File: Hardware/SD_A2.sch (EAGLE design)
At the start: 24 parts, among them IC1 74LS245N, IC2 LM1117DTX-3.3, IC3 28C64ASO, IC4 XC9572XL

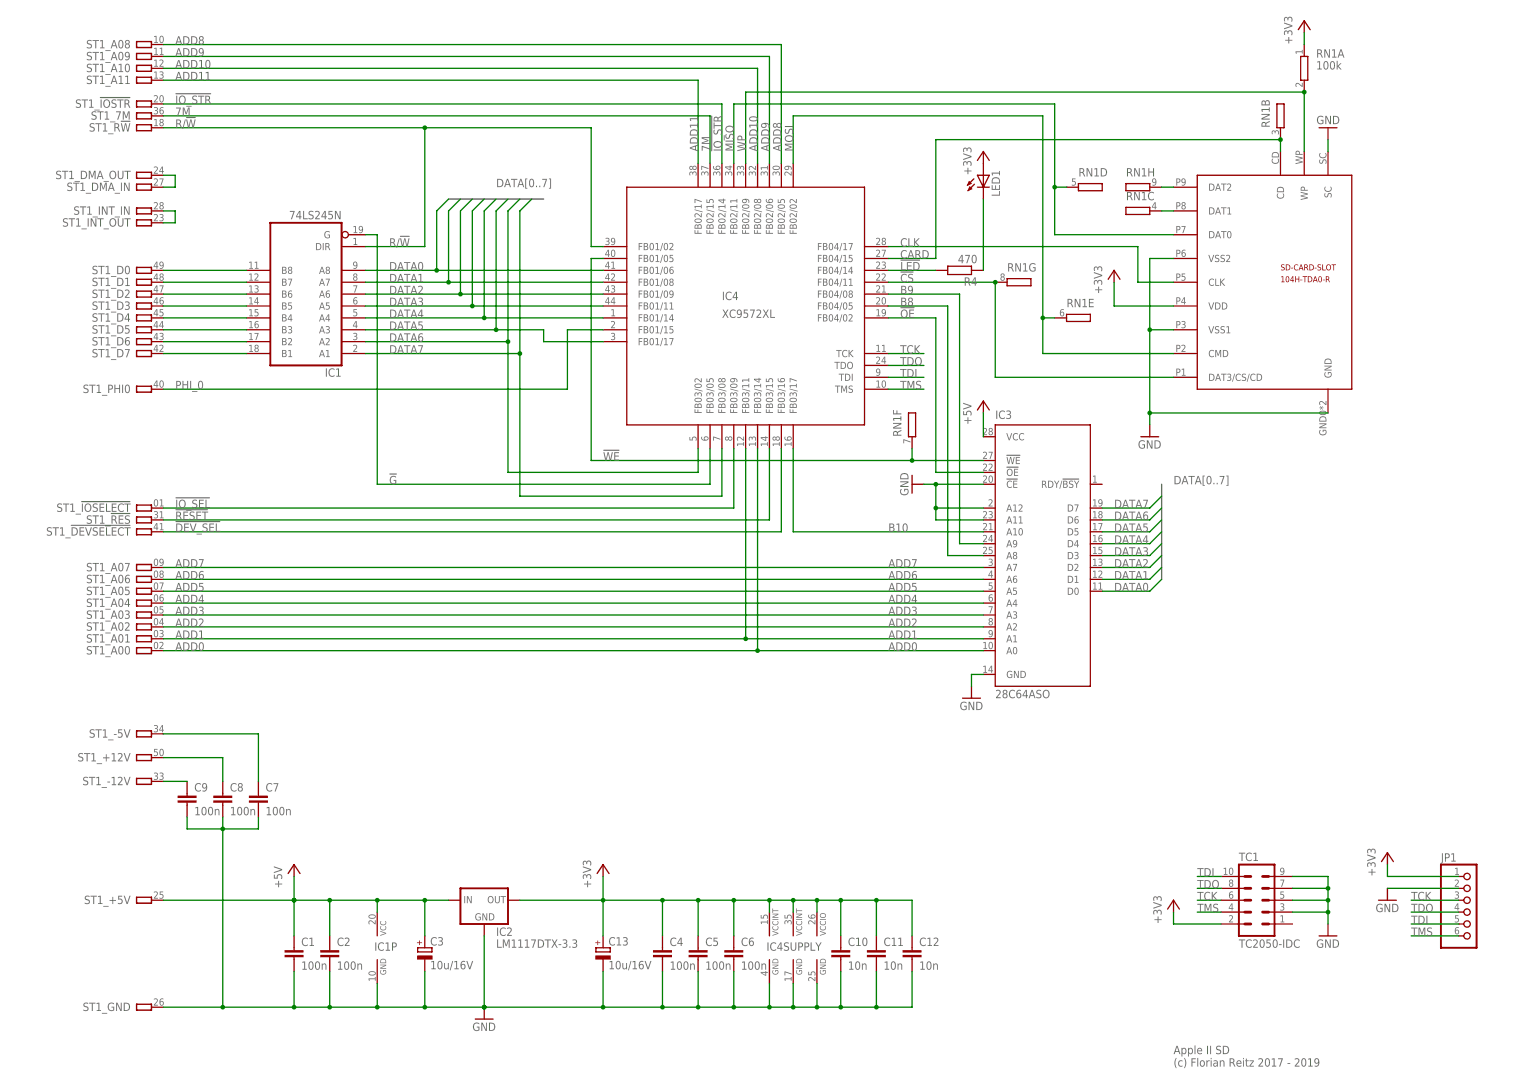
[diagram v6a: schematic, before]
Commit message: R/W jumper re-added
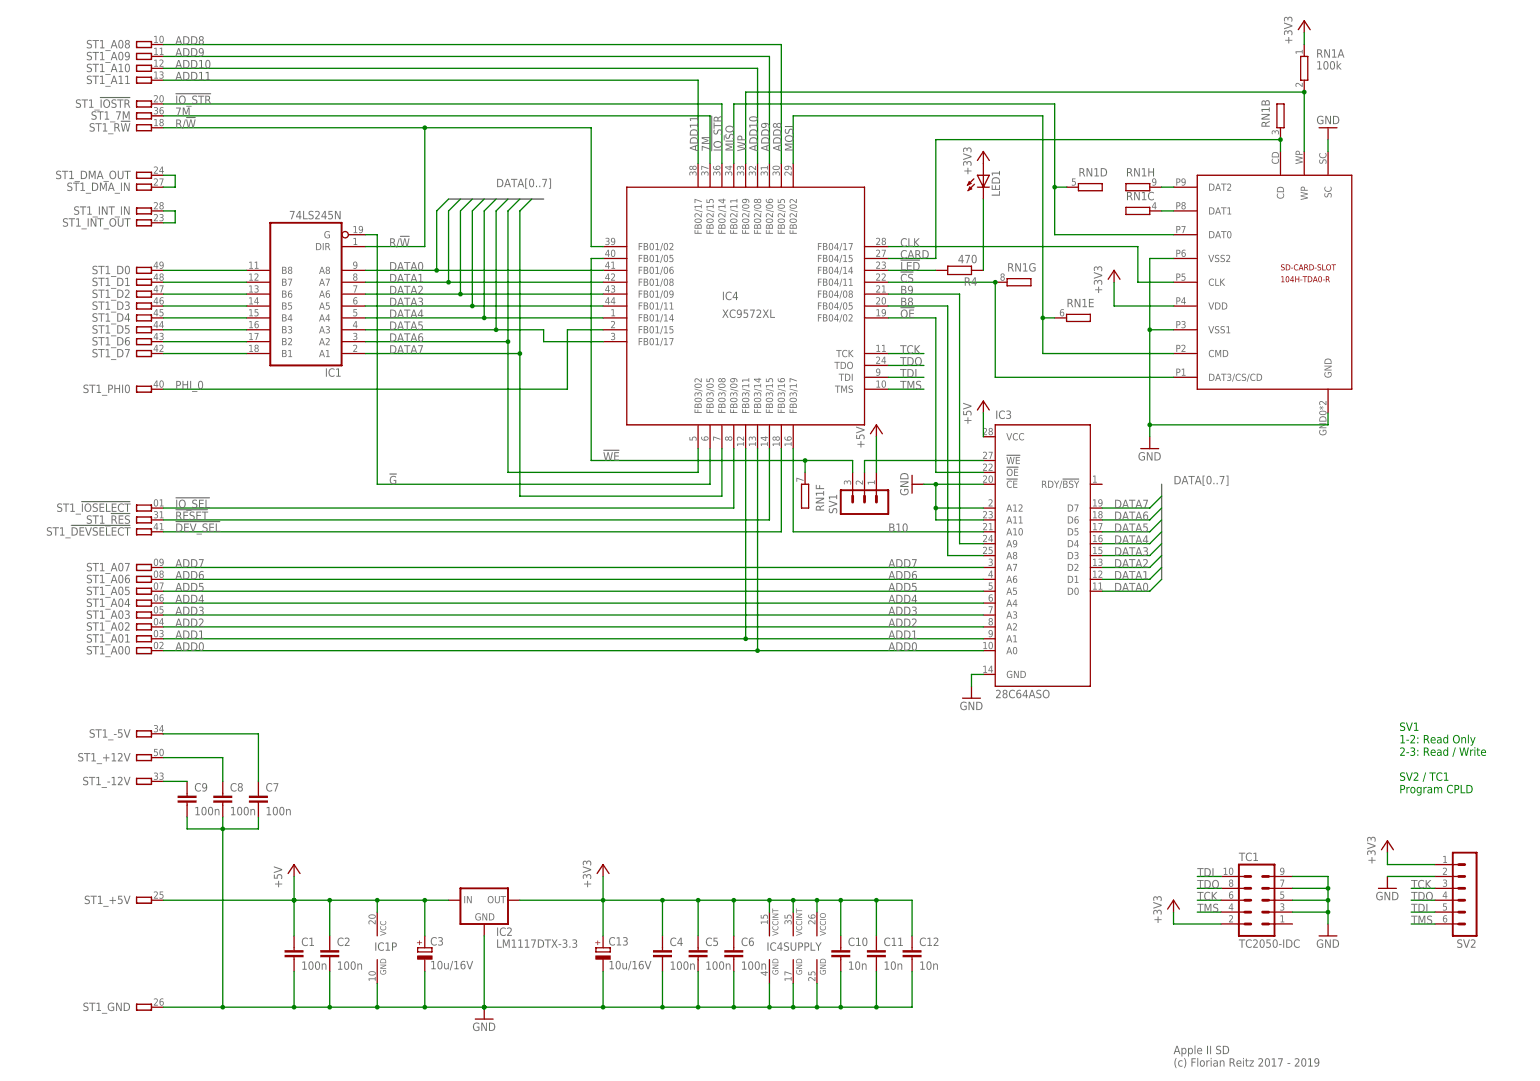
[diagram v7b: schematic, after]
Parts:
- removed JP1: (no value), pinhead:PINHD-1X6
- added SV1: (no value), con-lstb:MA03-1
- added SV2: (no value), con-lstb:MA06-1
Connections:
- new net N$1: IC3.!WE, SV1.2
- net !WE: now also SV1.3; no longer IC3.!WE
- net +3V3: now also SV2.1; no longer JP1.1
- net +5V: now also SV1.1
- net GND: now also SV2.2; no longer JP1.2
- net TCK: now also SV2.3; no longer JP1.3
- net TDI: now also SV2.5; no longer JP1.5
- net TDO: now also SV2.4; no longer JP1.4
- net TMS: now also SV2.6; no longer JP1.6
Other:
- note added: "SV1 1-2: Read Only 2-3: Read / Write SV2 / TC1 Program CPLD"
- moved on the sheet: RN1F
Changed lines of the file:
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@@
 <part name="C3" library="rcl@1" deviceset="CPOL-EU" device="A/3216-18R" value="10u/16V"/>
 <part name="C13" library="rcl@1" deviceset="CPOL-EU" device="A/3216-18R" value="10u/16V"/>
-<part name="JP1" library="pinhead" deviceset="PINHD-1X6" device=""/>
-<part name="+3V2" library="supply1" deviceset="+3V3" device=""/>
-<part name="GND2" library="supply1" deviceset="GND" device=""/>
 <part name="TC1" library="TagConnect" deviceset="TC2050-IDC" device=""/>
+<part name="SV1" library="con-lstb" deviceset="MA03-1" device=""/>
+<part name="SV2" library="con-lstb" deviceset="MA06-1" device=""/>
+<part name="P+2" library="supply1" deviceset="+5V" device=""/>
+<part name="+3V7" library="supply1" deviceset="+3V3" device=""/>
+<part name="GND3" library="supply1" deviceset="GND" device=""/>
 </parts>
 <sheets>
@@
 <text x="261.62" y="-27.94" size="1.778" layer="95" font="vector">Apple II SD
 (c) Florian Reitz 2017 - 2019</text>
+<text x="309.88" y="30.48" size="1.778" layer="91">SV1
+1-2: Read Only
+2-3: Read / Write
+SV2 / TC1
+Program CPLD</text>
 </plain>
 <instances>
@@
 <attribute name="NAME" x="174.625" y="-3.175" size="1.778" layer="95"/>
 </instance>
-<instance part="GND6" gate="1" x="256.54" y="106.68"/>
+<instance part="GND6" gate="1" x="256.54" y="104.14"/>
 <instance part="R4" gate="G$1" x="215.9" y="142.24" rot="R180"/>
 <instance part="+3V4" gate="G$1" x="220.98" y="167.64"/>
@@
 <instance part="C3" gate="G$1" x="101.6" y="-2.54"/>
 <instance part="C13" gate="G$1" x="139.7" y="-2.54"/>
-<instance part="RN1" gate="F" x="205.74" y="109.22" smashed="yes">
-<attribute name="NAME" x="203.454" y="106.68" size="1.778" layer="95" rot="R90"/>
+<instance part="RN1" gate="F" x="182.88" y="93.98" smashed="yes" rot="R180">
+<attribute name="NAME" x="185.166" y="96.52" size="1.778" layer="95" rot="R270"/>
 </instance>
-<instance part="JP1" gate="A" x="325.12" y="5.08"/>
-<instance part="+3V2" gate="G$1" x="307.34" y="17.78"/>
-<instance part="GND2" gate="1" x="307.34" y="7.62"/>
 <instance part="TC1" gate="A" x="279.4" y="7.62"/>
+<instance part="SV1" gate="G$1" x="195.58" y="91.44" rot="R90"/>
+<instance part="SV2" gate="1" x="325.12" y="7.62" rot="R180"/>
+<instance part="P+2" gate="1" x="198.12" y="109.22"/>
+<instance part="+3V7" gate="G$1" x="307.34" y="20.32"/>
+<instance part="GND3" gate="1" x="307.34" y="10.16"/>
 </instances>
 <busses>
@@
 <wire x1="256.54" y1="144.78" x2="256.54" y2="129.54" width="0.1524" layer="91"/>
 <pinref part="U$2" gate="G$1" pin="VSS1"/>
-<wire x1="256.54" y1="129.54" x2="256.54" y2="111.76" width="0.1524" layer="91"/>
-<wire x1="256.54" y1="111.76" x2="256.54" y2="109.22" width="0.1524" layer="91"/>
+<wire x1="256.54" y1="129.54" x2="256.54" y2="109.22" width="0.1524" layer="91"/>
+<wire x1="256.54" y1="109.22" x2="256.54" y2="106.68" width="0.1524" layer="91"/>
 <wire x1="261.62" y1="129.54" x2="256.54" y2="129.54" width="0.1524" layer="91"/>
 <junction x="256.54" y="129.54"/>
 <pinref part="U$2" gate="G$1" pin="GND"/>
-<wire x1="294.64" y1="111.76" x2="256.54" y2="111.76" width="0.1524" layer="91"/>
-<junction x="256.54" y="111.76"/>
+<wire x1="294.64" y1="111.76" x2="294.64" y2="109.22" width="0.1524" layer="91"/>
+<wire x1="294.64" y1="109.22" x2="256.54" y2="109.22" width="0.1524" layer="91"/>
+<junction x="256.54" y="109.22"/>
 </segment>
 <segment>
@@
 <wire x1="220.98" y1="55.88" x2="218.44" y2="55.88" width="0.1524" layer="91"/>
 <wire x1="218.44" y1="55.88" x2="218.44" y2="53.34" width="0.1524" layer="91"/>
-</segment>
-<segment>
-<pinref part="JP1" gate="A" pin="2"/>
-<pinref part="GND2" gate="1" pin="GND"/>
-<wire x1="322.58" y1="10.16" x2="307.34" y2="10.16" width="0.1524" layer="91"/>
 </segment>
 <segment>
@@
 <junction x="294.64" y="7.62"/>
 <junction x="294.64" y="5.08"/>
+</segment>
+<segment>
+<pinref part="GND3" gate="1" pin="GND"/>
+<pinref part="SV2" gate="1" pin="2"/>
+<wire x1="307.34" y1="12.7" x2="317.5" y2="12.7" width="0.1524" layer="91"/>
 </segment>
 </net>
@@
 <pinref part="IC3" gate="G$1" pin="VCC"/>
 <wire x1="220.98" y1="111.76" x2="220.98" y2="106.68" width="0.1524" layer="91"/>
+</segment>
+<segment>
+<pinref part="SV1" gate="G$1" pin="1"/>
+<wire x1="198.12" y1="99.06" x2="198.12" y2="106.68" width="0.1524" layer="91"/>
+<pinref part="P+2" gate="1" pin="+5V"/>
 </segment>
 </net>
@@
 </segment>
 <segment>
-<pinref part="+3V2" gate="G$1" pin="+3V3"/>
-<wire x1="307.34" y1="15.24" x2="307.34" y2="12.7" width="0.1524" layer="91"/>
-<pinref part="JP1" gate="A" pin="1"/>
-<wire x1="307.34" y1="12.7" x2="322.58" y2="12.7" width="0.1524" layer="91"/>
-</segment>
-<segment>
 <pinref part="TC1" gate="A" pin="2"/>
 <pinref part="+3V6" gate="G$1" pin="+3V3"/>
 <wire x1="271.78" y1="2.54" x2="261.62" y2="2.54" width="0.1524" layer="91"/>
 <wire x1="261.62" y1="2.54" x2="261.62" y2="5.08" width="0.1524" layer="91"/>
+</segment>
+<segment>
+<pinref part="+3V7" gate="G$1" pin="+3V3"/>
+<wire x1="307.34" y1="17.78" x2="307.34" y2="15.24" width="0.1524" layer="91"/>
+<pinref part="SV2" gate="1" pin="1"/>
+<wire x1="307.34" y1="15.24" x2="317.5" y2="15.24" width="0.1524" layer="91"/>
 </segment>
 </net>
@@
 </segment>
 <segment>
-<pinref part="JP1" gate="A" pin="3"/>
-<wire x1="322.58" y1="7.62" x2="312.42" y2="7.62" width="0.1524" layer="91"/>
-<label x="312.42" y="7.62" size="1.778" layer="95"/>
-</segment>
-<segment>
 <pinref part="TC1" gate="A" pin="6"/>
 <wire x1="271.78" y1="7.62" x2="266.7" y2="7.62" width="0.1524" layer="91"/>
 <label x="266.7" y="7.62" size="1.778" layer="95"/>
 </segment>
+<segment>
+<pinref part="SV2" gate="1" pin="3"/>
+<wire x1="317.5" y1="10.16" x2="312.42" y2="10.16" width="0.1524" layer="91"/>
+<label x="312.42" y="10.16" size="1.778" layer="95"/>
+</segment>
 </net>
 <net name="TDO" class="0">
@@
 </segment>
 <segment>
-<pinref part="JP1" gate="A" pin="4"/>
-<wire x1="322.58" y1="5.08" x2="312.42" y2="5.08" width="0.1524" layer="91"/>
-<label x="312.42" y="5.08" size="1.778" layer="95"/>
-</segment>
-<segment>
 <pinref part="TC1" gate="A" pin="8"/>
 <wire x1="271.78" y1="10.16" x2="266.7" y2="10.16" width="0.1524" layer="91"/>
 <label x="266.7" y="10.16" size="1.778" layer="95"/>
 </segment>
+<segment>
+<pinref part="SV2" gate="1" pin="4"/>
+<wire x1="317.5" y1="7.62" x2="312.42" y2="7.62" width="0.1524" layer="91"/>
+<label x="312.42" y="7.62" size="1.778" layer="95"/>
+</segment>
 </net>
 <net name="TDI" class="0">
@@
 </segment>
 <segment>
-<pinref part="JP1" gate="A" pin="5"/>
-<wire x1="322.58" y1="2.54" x2="312.42" y2="2.54" width="0.1524" layer="91"/>
-<label x="312.42" y="2.54" size="1.778" layer="95"/>
-</segment>
-<segment>
 <pinref part="TC1" gate="A" pin="10"/>
 <wire x1="271.78" y1="12.7" x2="266.7" y2="12.7" width="0.1524" layer="91"/>
 <label x="266.7" y="12.7" size="1.778" layer="95"/>
 </segment>
+<segment>
+<pinref part="SV2" gate="1" pin="5"/>
+<wire x1="317.5" y1="5.08" x2="312.42" y2="5.08" width="0.1524" layer="91"/>
+<label x="312.42" y="5.08" size="1.778" layer="95"/>
+</segment>
 </net>
 <net name="TMS" class="0">
@@
 </segment>
 <segment>
-<pinref part="JP1" gate="A" pin="6"/>
-<wire x1="322.58" y1="0" x2="312.42" y2="0" width="0.1524" layer="91"/>
-<label x="312.42" y="0" size="1.778" layer="95"/>
-</segment>
-<segment>
 <pinref part="TC1" gate="A" pin="4"/>
 <wire x1="271.78" y1="5.08" x2="266.7" y2="5.08" width="0.1524" layer="91"/>
 <label x="266.7" y="5.08" size="1.778" layer="95"/>
+</segment>
+<segment>
+<pinref part="SV2" gate="1" pin="6"/>
+<wire x1="317.5" y1="2.54" x2="312.42" y2="2.54" width="0.1524" layer="91"/>
+<label x="312.42" y="2.54" size="1.778" layer="95"/>
 </segment>
 </net>
@@
 <wire x1="139.7" y1="144.78" x2="137.16" y2="144.78" width="0.1524" layer="91"/>
 <wire x1="137.16" y1="144.78" x2="137.16" y2="101.6" width="0.1524" layer="91"/>
-<wire x1="137.16" y1="101.6" x2="205.74" y2="101.6" width="0.1524" layer="91"/>
+<wire x1="137.16" y1="101.6" x2="182.88" y2="101.6" width="0.1524" layer="91"/>
 <label x="139.7" y="101.6" size="1.778" layer="95"/>
-<pinref part="IC3" gate="G$1" pin="!WE"/>
 <pinref part="RN1" gate="F" pin="2"/>
-<wire x1="205.74" y1="101.6" x2="220.98" y2="101.6" width="0.1524" layer="91"/>
-<wire x1="205.74" y1="104.14" x2="205.74" y2="101.6" width="0.1524" layer="91"/>
-<junction x="205.74" y="101.6"/>
+<wire x1="182.88" y1="99.06" x2="182.88" y2="101.6" width="0.1524" layer="91"/>
+<pinref part="SV1" gate="G$1" pin="3"/>
+<wire x1="182.88" y1="101.6" x2="193.04" y2="101.6" width="0.1524" layer="91"/>
+<wire x1="193.04" y1="101.6" x2="193.04" y2="99.06" width="0.1524" layer="91"/>
+<junction x="182.88" y="101.6"/>
 </segment>
 </net>
@@
 </segment>
 </net>
+<net name="N$1" class="0">
+<segment>
+<pinref part="SV1" gate="G$1" pin="2"/>
+<wire x1="195.58" y1="99.06" x2="195.58" y2="101.6" width="0.1524" layer="91"/>
+<pinref part="IC3" gate="G$1" pin="!WE"/>
+<wire x1="195.58" y1="101.6" x2="220.98" y2="101.6" width="0.1524" layer="91"/>
+</segment>
+</net>
